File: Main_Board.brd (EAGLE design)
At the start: 160.3 x 95.4 mm, 227 parts, among them J1 SERVO, J2 5.5x2.1mm Barrel, J3 9.7uH, J4 BATTERY, J5 SPEAKER, J6 SDIO-SDCARD, J7 header, P1 MOTOR_HEADER, P2 MOTOR_HEADER, P3 JTAG, Q1 SI9933CDY-PFET, Q2 CSD17308Q3, Q3 CSD17308Q3, Q4 CSD17308Q3, Q5 CSD17308Q3, Q6 CSD17308Q3, Q7 CSD17308Q3, Q8 CSD17308Q3, U1 LMS8117, U10 IMU, U11 LTC3122-MSOP, U12 CBAT54S-SOT23-3, U13 BQ2947, U14 TPA2005D1DGN, U15 BQ40Z60, U2 5V_BUCK_REG, U3 BTM7752G, U4 BTM7752G, U5 SN74LV4T125, U6 SN74LV4T125, U7 STM32F405RGT6, U8 RN4020RN4020, U9 BQ51013B-20VQFN

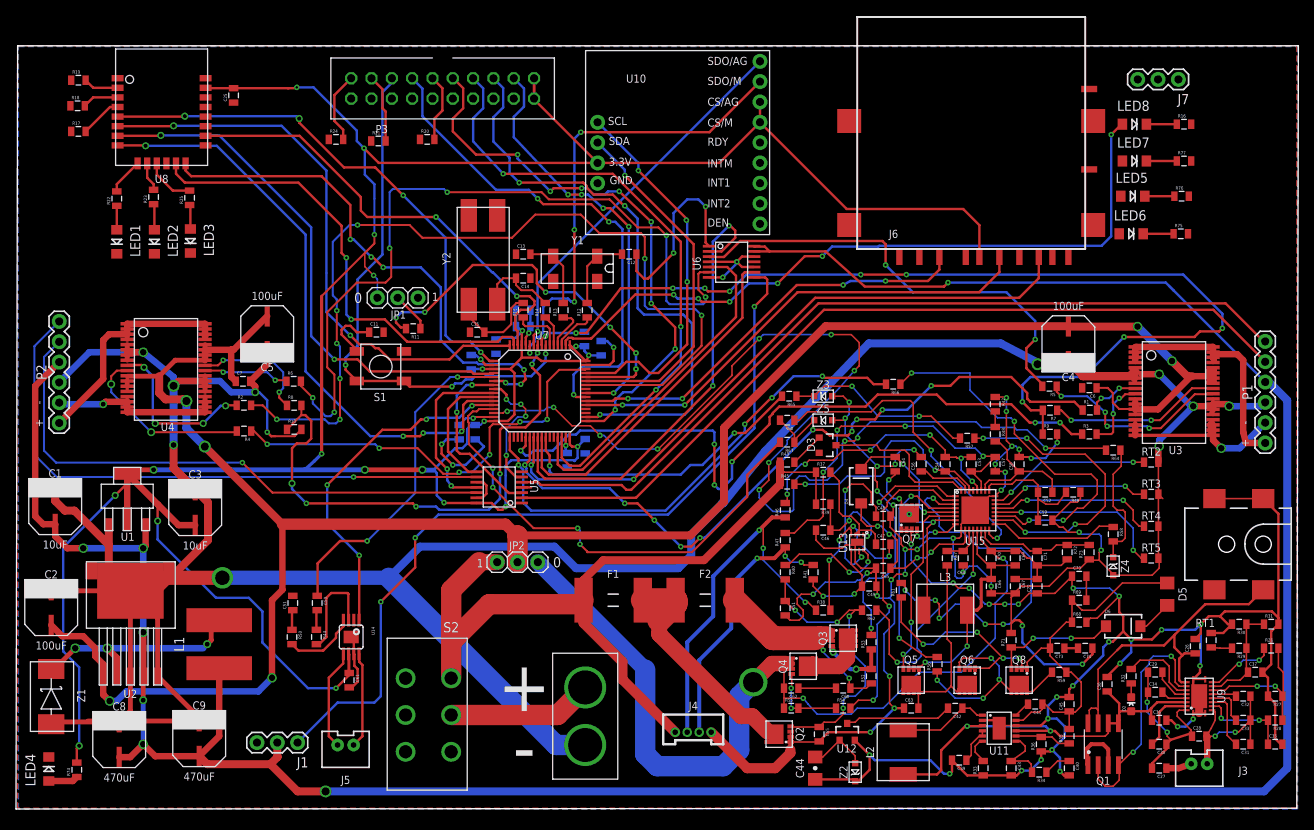
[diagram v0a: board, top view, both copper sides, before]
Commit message: Down to 33 clearance errors
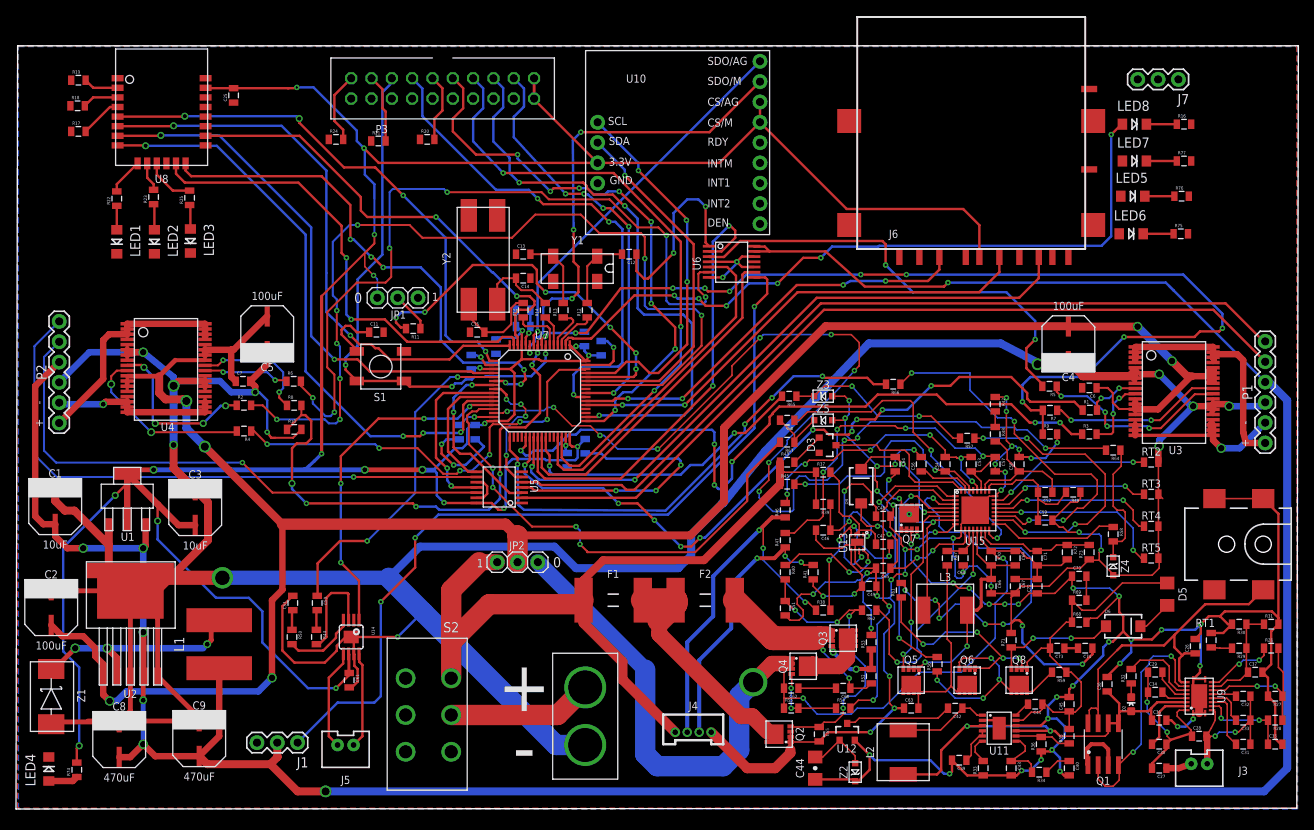
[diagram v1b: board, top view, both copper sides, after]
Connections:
- net GND: now also U2.P$7, U2.P$8
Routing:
- net GND: track 738.7 -> 801.0 mm, vias 53 -> 57

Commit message: Removed ALL violations
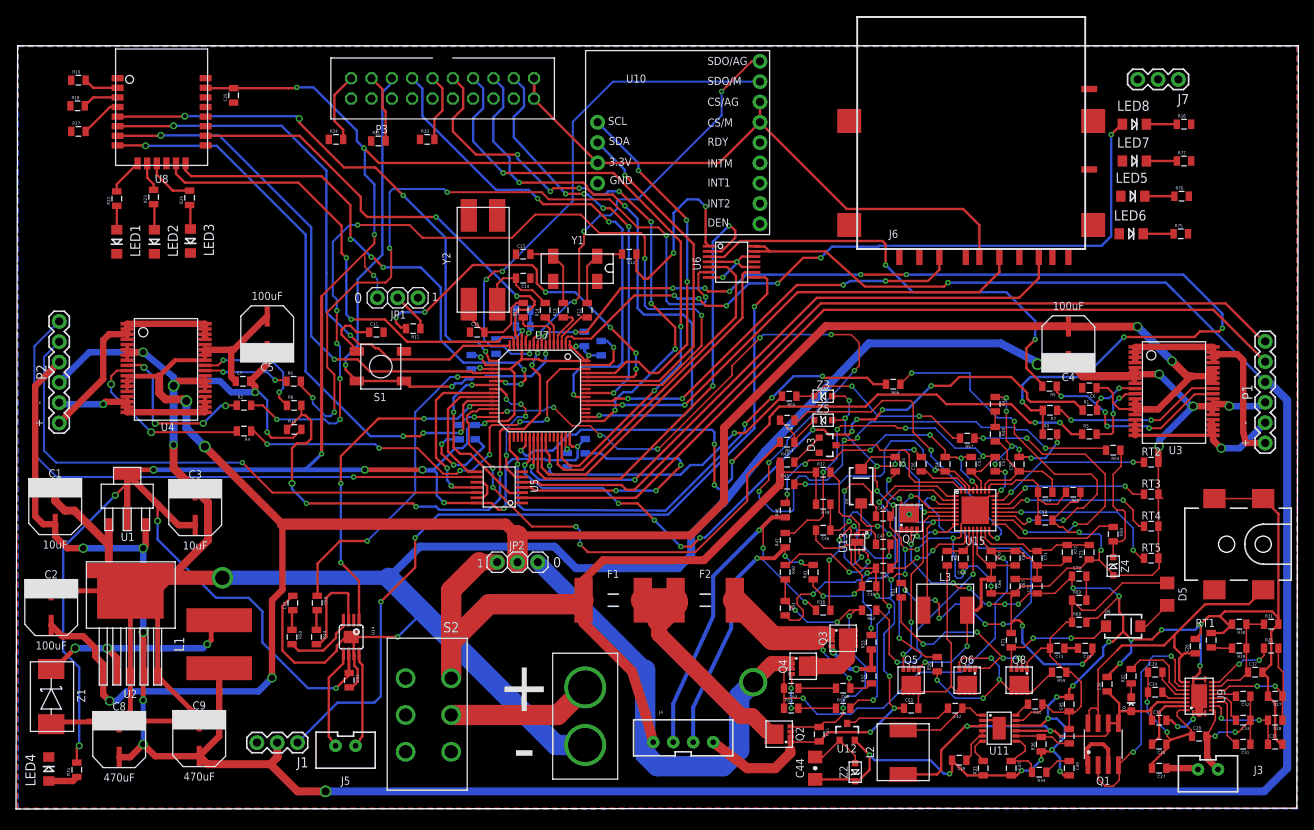
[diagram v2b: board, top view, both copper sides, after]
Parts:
- J4: device SparkFun-Connectors:1X04-1.5MM_JST -> BB8:JST-4-PTH-VERT
- moved J3 1.30 mm to (149.0, 4.40)
- moved J4 1.22 mm to (83.4, 8.90)
- moved J5 0.10 mm to (41.2, 7.35)
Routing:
- net IMU_SDO_M: track 58.4 -> 65.4 mm, vias 4 -> 3
- net IMU_SDO_AG: track 47.2 -> 50.3 mm, vias 1 -> 4
- net AC2: track 19.6 -> 20.9 mm
- net GND: track 801.0 -> 800.0 mm
- net N$116: track 46.9 -> 47.9 mm
- net N$59: track 3.19 -> 4.01 mm
- net N$33: track 33.9 -> 34.5 mm
- net 12V_BAT: track 101.7 -> 101.1 mm

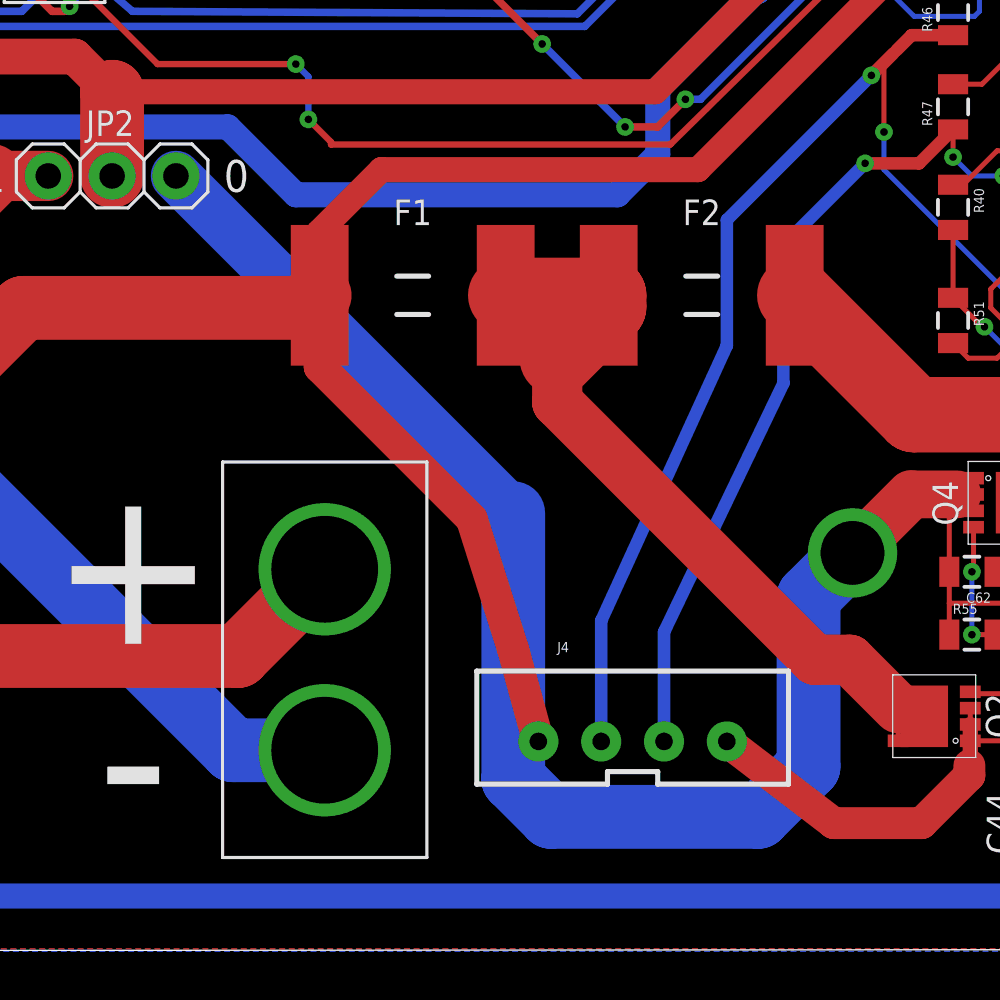
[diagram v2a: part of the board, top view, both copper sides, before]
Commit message: Fixed overlap issue caused by resizing
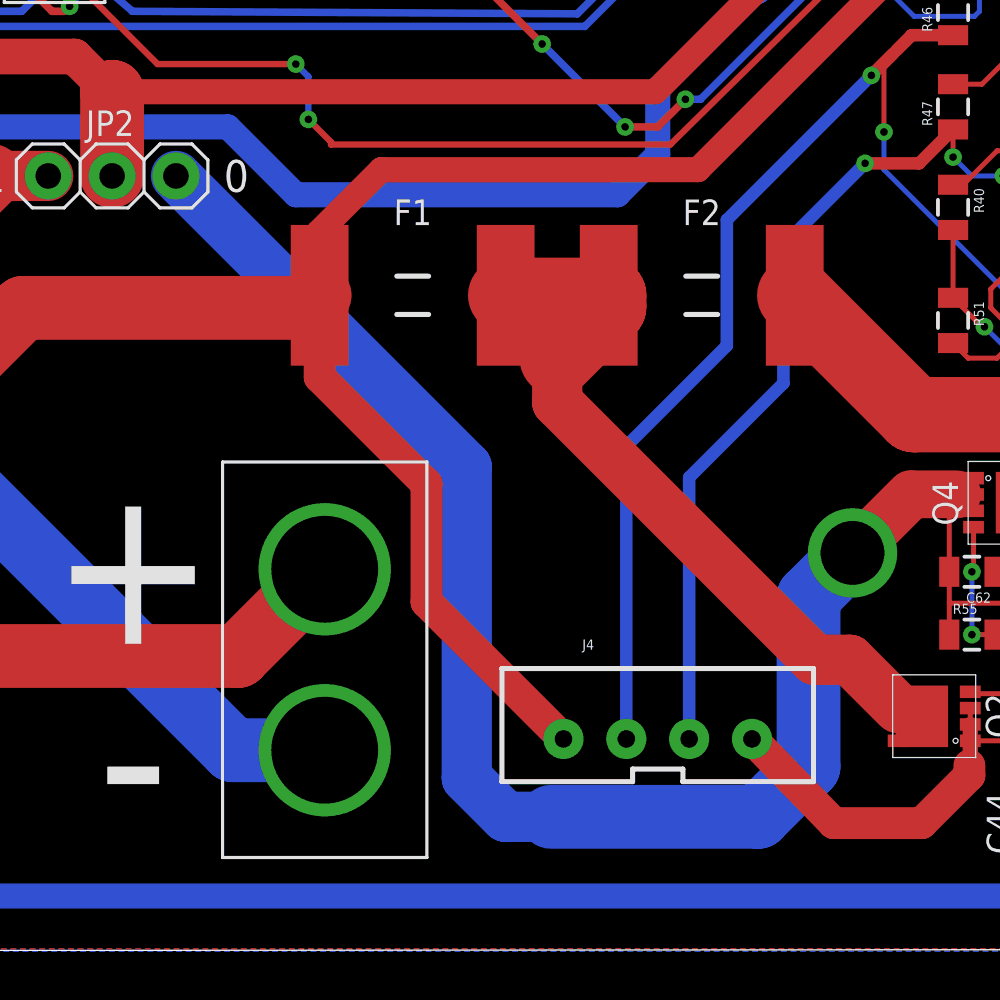
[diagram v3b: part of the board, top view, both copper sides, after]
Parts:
- moved J4 1.00 mm to (84.4, 9.00)
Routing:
- net 12V_CC: track 127.1 -> 128.2 mm
- net 12V_BAT: track 101.1 -> 102.1 mm
- net GND: track 800.0 -> 799.3 mm
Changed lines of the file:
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@@
 <element name="R42" library="SparkFun-Resistors" package="0805" value="5m" x="122.4" y="50.6" rot="R270"/>
 <element name="R40" library="SparkFun-Resistors" package="0805" value="5.1k" x="96.15" y="29.6" rot="R270"/>
-<element name="J4" library="BB8" package="JST-4-PTH-VERT" value="BATTERY" x="83.4" y="8.9"/>
+<element name="J4" library="BB8" package="JST-4-PTH-VERT" value="BATTERY" x="84.4" y="9"/>
 <element name="R39" library="SparkFun-Resistors" package="0805" value="100" x="100.9" y="38.1" rot="R180"/>
 <element name="C46" library="SparkFun-Capacitors" package="0805" value="0.1uF" x="100.9" y="34.85" rot="R180"/>
@@
 <wire x1="125.4" y1="23.6" x2="124.8" y2="23.6" width="0.3" layer="1"/>
 <wire x1="124.8" y1="23.6" x2="124.4" y2="23.2" width="0.3" layer="1"/>
-<wire x1="87.15" y1="8.35" x2="91.4" y2="5.1" width="1.27" layer="1"/>
+<wire x1="88.15" y1="8.45" x2="91.4" y2="5.1" width="1.27" layer="1"/>
 <wire x1="91.4" y1="5.1" x2="94.9" y2="5.1" width="1.27" layer="1"/>
 <wire x1="94.9" y1="5.1" x2="96.8" y2="7" width="1.27" layer="1"/>
@@
 <wire x1="54.4" y1="27.35" x2="54.4" y2="20.85" width="2.54" layer="1"/>
 <wire x1="57.9" y1="30.85" x2="60.15" y2="30.85" width="2" layer="1"/>
-<wire x1="79.65" y1="8.35" x2="78.65" y2="12" width="1.27" layer="1"/>
-<wire x1="78.65" y1="12" x2="77" y2="17.2" width="1.27" layer="1"/>
-<wire x1="77" y1="17.2" x2="70.95" y2="23.25" width="1.27" layer="1"/>
-<wire x1="70.95" y1="23.25" x2="70.95" y2="26.1" width="1.27" layer="1"/>
+<wire x1="70.95" y1="26.1" x2="70.95" y2="22.85" width="1.27" layer="1"/>
+<wire x1="70.95" y1="22.85" x2="75.2" y2="18.6" width="1.27" layer="1"/>
+<wire x1="75.2" y1="18.6" x2="75.2" y2="13.9" width="1.27" layer="1"/>
+<wire x1="75.2" y1="13.9" x2="80.65" y2="8.45" width="1.27" layer="1"/>
 </signal>
 <signal name="N$105">
@@
 <wire x1="93.4" y1="35.35" x2="93.775" y2="35.725" width="0.2" layer="1"/>
 <wire x1="93.775" y1="35.725" x2="93.9" y2="35.85" width="0.2" layer="1"/>
-<wire x1="82.15" y1="8.35" x2="82.15" y2="13.15" width="0.5" layer="16"/>
-<wire x1="82.15" y1="13.15" x2="87.15" y2="24.1" width="0.5" layer="16"/>
 <wire x1="87.15" y1="24.1" x2="87.15" y2="29.1" width="0.5" layer="16"/>
 <wire x1="87.15" y1="29.1" x2="92.9" y2="34.85" width="0.5" layer="16"/>
 <via x="92.9" y="34.85" extent="1-16" drill="0.3"/>
 <wire x1="92.9" y1="34.85" x2="93.775" y2="35.725" width="0.5" layer="1"/>
+<wire x1="87.15" y1="24.1" x2="83.15" y2="20.1" width="0.5" layer="16"/>
+<wire x1="83.15" y1="20.1" x2="83.15" y2="8.45" width="0.5" layer="16"/>
 </signal>
 <signal name="N$118">
@@
 <wire x1="92.65" y1="31.35" x2="94.8" y2="31.35" width="0.5" layer="1"/>
 <wire x1="94.8" y1="31.35" x2="96.15" y2="32.7" width="0.5" layer="1"/>
-<wire x1="84.65" y1="8.35" x2="84.65" y2="12.7" width="0.5" layer="16"/>
-<wire x1="84.65" y1="12.7" x2="89.4" y2="22.6" width="0.5" layer="16"/>
 <wire x1="89.4" y1="22.6" x2="89.4" y2="28.1" width="0.5" layer="16"/>
+<wire x1="89.4" y1="22.6" x2="85.65" y2="18.85" width="0.5" layer="16"/>
+<wire x1="85.65" y1="18.85" x2="85.65" y2="8.45" width="0.5" layer="16"/>
 </signal>
 <signal name="N$40">
@@
 <wire x1="96" y1="17.86" x2="96" y2="15.1" width="0.2" layer="1"/>
 <contactref element="JP2" pad="3"/>
-<wire x1="78.65" y1="17.43" x2="78.65" y2="6.85" width="2.54" layer="16"/>
-<wire x1="78.65" y1="6.85" x2="80.15" y2="5.35" width="2.54" layer="16"/>
 <wire x1="80.15" y1="5.35" x2="88.4" y2="5.35" width="2.54" layer="16"/>
 <wire x1="88.4" y1="5.35" x2="90.4" y2="7.35" width="2.54" layer="16"/>
@@
 <via x="92.15" y="15.85" extent="1-16" drill="2.54"/>
 <wire x1="92.15" y1="15.85" x2="94.48" y2="18.18" width="1.9304" layer="1"/>
-<wire x1="65.23" y1="30.85" x2="78.65" y2="17.43" width="2" layer="16"/>
 <wire x1="96.32" y1="18.18" x2="94.48" y2="18.18" width="1.9" layer="1"/>
+<wire x1="65.23" y1="30.85" x2="76.8" y2="19.28" width="2" layer="16"/>
+<wire x1="76.8" y1="19.28" x2="76.8" y2="6.9" width="2" layer="16"/>
+<wire x1="76.8" y1="6.9" x2="78.35" y2="5.35" width="2" layer="16"/>
+<wire x1="78.35" y1="5.35" x2="80.15" y2="5.35" width="2" layer="16"/>
 </signal>
 <signal name="N$29">

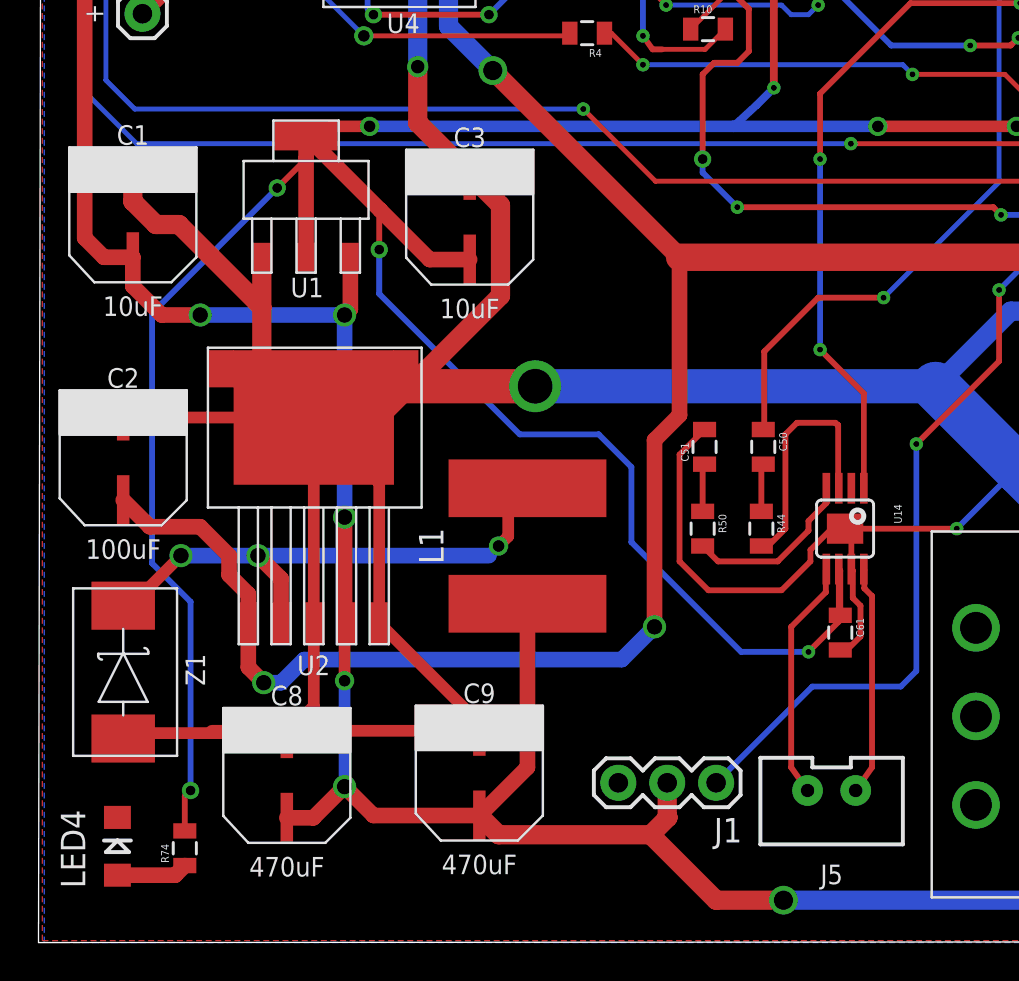
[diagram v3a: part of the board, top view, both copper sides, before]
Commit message: Modified capacitor sizes
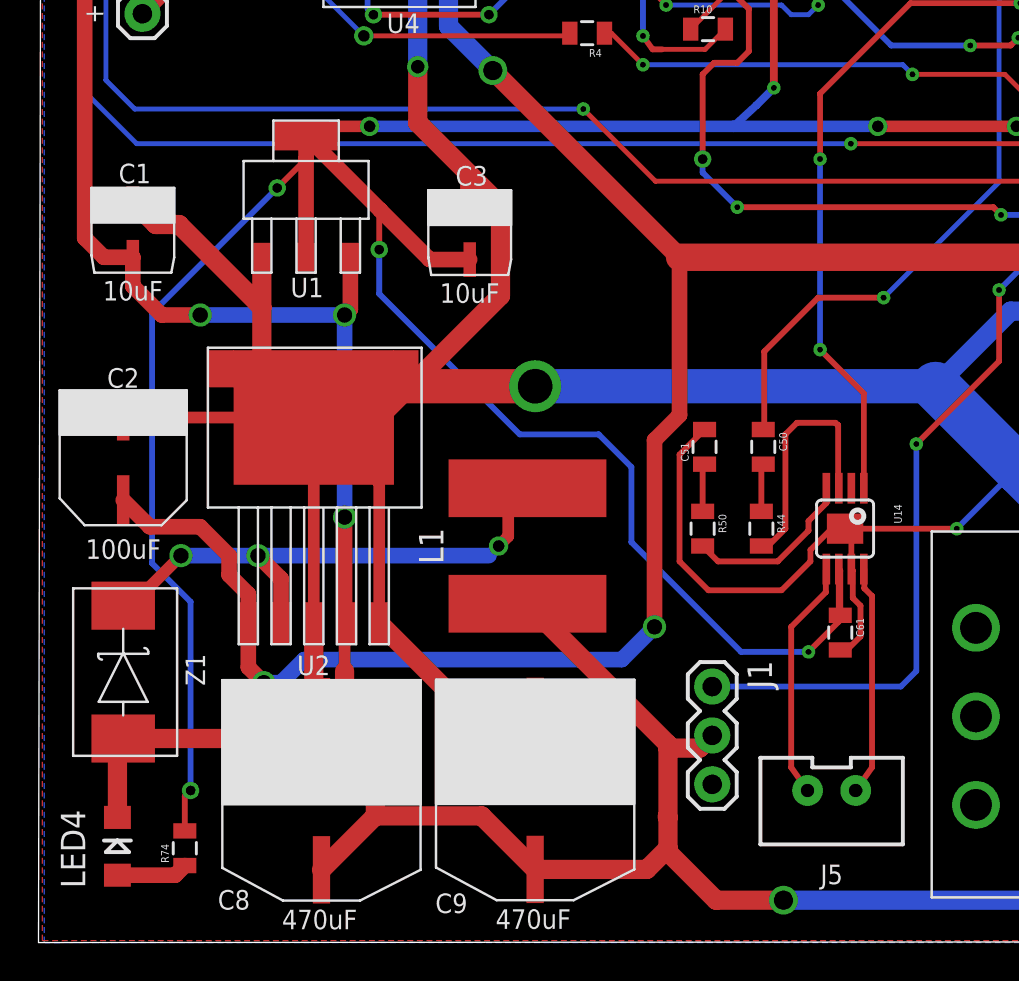
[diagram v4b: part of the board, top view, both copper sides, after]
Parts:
- C1, C3: device BB8:RADIAL_CAN_SMD -> BB8:RADIAL_CAN_SMD-B
- C2, C4, C5: device BB8:RADIAL_CAN_SMD -> BB8:RADIAL_CAN_SMD-D8
- C8, C9: device BB8:RADIAL_CAN_SMD -> BB8:RADIAL_CAN_SMD-G
- moved J1 5.00 mm to (35.0, 13.3), turned to 270 degrees
- moved C9 4.03 mm to (25.8, 3.80)
- moved C8 3.24 mm to (14.7, 3.78)
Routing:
- net 5V: track 353.4 -> 358.4 mm, vias 7 -> 5
- net SERVO_PWM_5: track 103.5 -> 101.6 mm
- net GND: track 799.3 -> 797.4 mm
